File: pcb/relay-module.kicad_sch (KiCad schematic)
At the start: 12 parts

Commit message: initial checkin
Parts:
- added C1: .1uF, Capacitor_SMD:C_0603_1608Metric, symbol Device:C
- added D1: BAT48JFILM, Diode_SMD:D_SOD-323, symbol Diode:BAT48JFILM
- added J1: AVR-UPDI-6, Connector_PinHeader_2.54mm:PinHeader_2x03_P2.54mm_Vertical, symbol Connector:AVR-UPDI-6
- added J2: QWICC, Connector_JST:JST_SH_SM04B-SRSS-TB_1x04-1MP_P1.00mm_Horizontal, symbol CRGM Connector:QWIIC
- added J3: Power, Connector_JST:JST_SH_SM04B-SRSS-TB_1x04-1MP_P1.00mm_Horizontal, symbol CRGM Connector:JST-SH-4
- added JP1: Jumper_3_Open, Jumper:SolderJumper-3_P1.3mm_Open_RoundedPad1.0x1.5mm_NumberLabels, symbol Jumper:Jumper_3_Open
- added K1: PR24-5V-900-1A, CRG Makes:RELAY_PR24-5V-900-1A, symbol CRG Makes:PR24-5V-900-1A
- added MOV1: V250LA40BP, CRG Makes:V250LA40BP, symbol CRG Makes:MOV20D331K
- added P1, P2, P3, P4: MountingHole_Pad, MountingHole:MountingHole_3.2mm_M3_ISO14580_Pad, symbol Mechanical:MountingHole_Pad
- added Q1: MMBT3904, Package_TO_SOT_SMD:SOT-23, symbol Transistor_BJT:MMBT3904
- added R1, R2: 220, Resistor_SMD:R_0603_1608Metric, symbol Device:R_US
- added R3, R4: 10K, Resistor_SMD:R_0603_1608Metric, symbol Device:R_US
- added S1, S2: ~, CRGM Symbols:HIGH-VOLTAGE-5MM, symbol CRGM Symbols:High Voltage
- added U2: ATtiny1616-M, Package_DFN_QFN:VQFN-20-1EP_3x3mm_P0.4mm_EP1.7x1.7mm, symbol MCU_Microchip_ATtiny:ATtiny1616-M
- added U3: LTV-356T, Package_SO:SO-4_4.4x3.6mm_P2.54mm, symbol Isolator:LTV-356T
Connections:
- new net: R1.2, U3.1
- new net: R2.1, U3.3
- new net: JP1.1 (A), R3.2
- new net: JP1.3 (B), R4.2
- new net: Q1.1 (B), R2.2
- new net +3.3V: C1.1, J1.2 (VCC), J2.2, J3.4, JP1.2 (C), U2.4 (VCC), U3.4
- new net +5V: D1.1 (K), J3.1, K1.A1 (COIL1)
- new net GND: C1.2, J1.6 (GND), J2.1, J3.2, J3.3, Q1.2 (E), U2.21 (GND), U2.3 (GND), U3.2
- new net LOAD_IN: K1.COM_1 (COM1), P3.1
- new net LOAD_OUT: K1.NO, MOV1.P$1, P4.1
- new net NEUTRAL: MOV1.P$2, P1.1, P2.1
- new net RELAY_CONTROL: D1.2 (A), K1.A2 (COIL2), Q1.3 (C)
- new net RELAY_CTRL: R1.1, U2.15 (PC0)
- new net SCL: J2.4, R3.1, U2.14 (PB0)
- new net SDA: J2.3, R4.1, U2.13 (PB1)
- new net UPDI: J1.1 (DATA), U2.19 (~{RESET}/PA0)
- no-connect marks 0 -> 15
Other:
- removed sheet I2C Interface
- removed sheet Power
- removed sheet Relay
- note added: "Power Connector"
- note added: "Programming"
- note added: "QWICC / I2C"
- note added: "Relay"
- note added: "uC"
- moved on the sheet: FID1, FID2, FID3, H1, H2, H3, H4

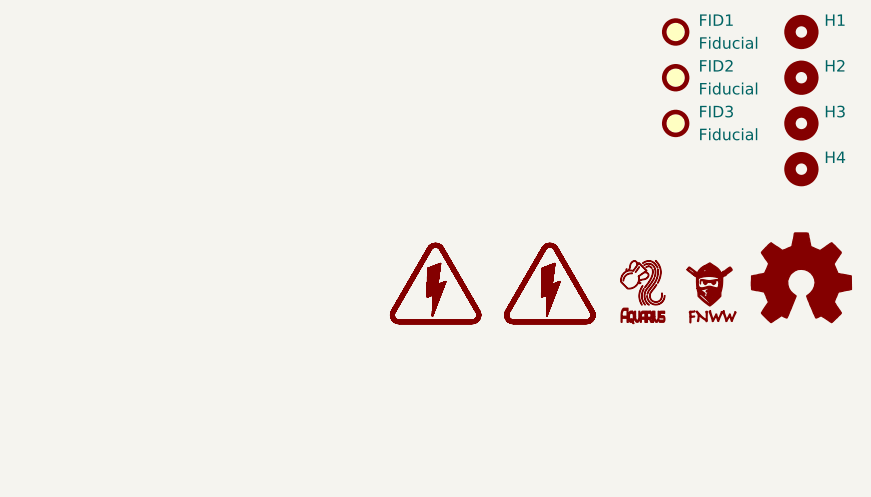
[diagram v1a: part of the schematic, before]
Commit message: Updated silkscreen
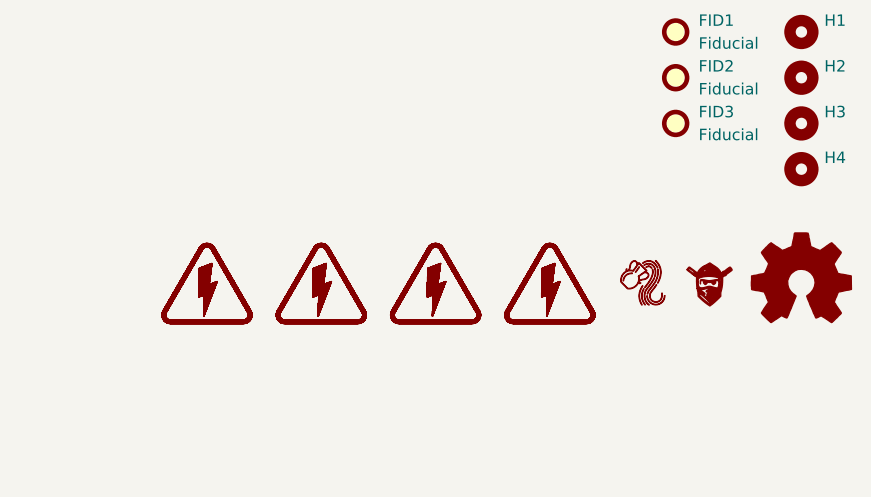
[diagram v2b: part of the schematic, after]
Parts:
- removed LOGO2: ~, CRGM Logos:Aquarius Name 2mmx5mm, symbol CRGM Logos:Aquarius Name
- removed LOGO4: ~, CRGM Logos:FNWW Name 2mmx5mm, symbol CRGM Logos:FNWW Name
- added S3, S4: ~, CRGM Symbols:HIGH-VOLTAGE-5MM, symbol CRGM Symbols:High Voltage
- LOGO1: footprint CRGM Logos:Aquarius Logo 5mm -> CRGM Logos:Aquarius Logo 10mm
- LOGO3: footprint CRGM Logos:FNWW Face 5mm -> CRGM Logos:FNWW Face 10mm
- LOGO5: footprint Symbol:OSHW-Symbol_6.7x6mm_SilkScreen -> Symbol:OSHW-Logo_5.7x6mm_SilkScreen
- S1, S2: now left out of the parts list
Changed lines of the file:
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@@
+	)
+	(symbol
+		(lib_id "CRGM Symbols:High Voltage")
+		(at 212.09 173.99 0)
+		(unit 1)
+		(exclude_from_sim no)
+		(in_bom no)
+		(on_board yes)
+		(dnp no)
+		(fields_autoplaced yes)
+		(property "Reference" "S3"
+			(at 212.09 183.388 0)
+			(effects
+				(font
+					(size 1.27 1.27)
+				)
+				(hide yes)
+			)
+		)
+		(property "Value" "~"
+			(at 212.09 173.99 0)
+			(effects
+				(font
+					(size 1.27 1.27)
+				)
+				(hide yes)
+			)
+		)
+		(property "Footprint" "CRGM Symbols:HIGH-VOLTAGE-5MM"
+			(at 213.36 181.102 0)
+			(effects
+				(font
+					(size 1.27 1.27)
+				)
+				(hide yes)
+			)
+		)
+		(property "Datasheet" ""
+			(at 212.09 173.99 0)
+			(effects
+				(font
+					(size 1.27 1.27)
+				)
+				(hide yes)
+			)
+		)
+		(property "Description" ""
+			(at 212.09 173.99 0)
+			(effects
+				(font
+					(size 1.27 1.27)
+				)
+				(hide yes)
+			)
+		)
+		(instances
+			(project "relay-module"
+				(path "/445c1fff-2e1a-48b1-a91f-a137832edebf"
+					(reference "S3")
+					(unit 1)
+				)
+			)
+		)
 	)
 	(symbol
@@
 			)
 		)
-		(property "Footprint" "CRGM Logos:Aquarius Logo 5mm"
+		(property "Footprint" "CRGM Logos:Aquarius Logo 10mm"
 			(at 261.874 179.578 0)
 			(effects
@@
 		(unit 1)
 		(exclude_from_sim no)
-		(in_bom yes)
+		(in_bom no)
 		(on_board yes)
 		(dnp no)
@@
 			)
 		)
-		(property "Footprint" "Symbol:OSHW-Symbol_6.7x6mm_SilkScreen"
+		(property "Footprint" "Symbol:OSHW-Logo_5.7x6mm_SilkScreen"
 			(at 278.13 173.99 0)
 			(effects
@@
 				(path "/445c1fff-2e1a-48b1-a91f-a137832edebf"
 					(reference "#PWR04")
-					(unit 1)
-				)
-			)
-		)
-	)
-	(symbol
-		(lib_id "CRGM Logos:Aquarius Name")
-		(at 260.3903 178.523 0)
-		(unit 1)
-		(exclude_from_sim no)
-		(in_bom no)
-		(on_board yes)
-		(dnp no)
-		(fields_autoplaced yes)
-		(property "Reference" "LOGO2"
-			(at 260.1363 179.539 0)
-			(effects
-				(font
-					(size 1.27 1.27)
-				)
-				(hide yes)
-			)
-		)
-		(property "Value" "~"
-			(at 258.1043 176.745 0)
-			(effects
-				(font
-					(size 1.27 1.27)
-				)
-				(hide yes)
-			)
-		)
-		(property "Footprint" "CRGM Logos:Aquarius Name 2mmx5mm"
-			(at 261.4063 181.063 0)
-			(effects
-				(font
-					(size 1.27 1.27)
-				)
-				(hide yes)
-			)
-		)
-		(property "Datasheet" ""
-			(at 258.1043 176.745 0)
-			(effects
-				(font
-					(size 1.27 1.27)
-				)
-				(hide yes)
-			)
-		)
-		(property "Description" ""
-			(at 258.1043 176.745 0)
-			(effects
-				(font
-					(size 1.27 1.27)
-				)
-				(hide yes)
-			)
-		)
-		(property "MPN" ""
-			(at 260.3903 178.523 0)
-			(effects
-				(font
-					(size 1.27 1.27)
-				)
-			)
-		)
-		(instances
-			(project ""
-				(path "/445c1fff-2e1a-48b1-a91f-a137832edebf"
-					(reference "LOGO2")
 					(unit 1)
 				)
@@
 	)
 	(symbol
-		(lib_id "CRGM Logos:FNWW Name")
-		(at 267.97 177.8 0)
-		(unit 1)
-		(exclude_from_sim no)
-		(in_bom no)
-		(on_board yes)
-		(dnp no)
-		(fields_autoplaced yes)
-		(property "Reference" "LOGO4"
-			(at 268.224 179.578 0)
-			(effects
-				(font
-					(size 1.27 1.27)
-				)
-				(hide yes)
-			)
-		)
-		(property "Value" "~"
-			(at 267.991 183.4101 0)
-			(effects
-				(font
-					(size 1.27 1.27)
-				)
-				(hide yes)
-			)
-		)
-		(property "Footprint" "CRGM Logos:FNWW Name 2mmx5mm"
-			(at 271.526 182.118 0)
-			(effects
-				(font
-					(size 1.27 1.27)
-				)
-				(hide yes)
-			)
-		)
-		(property "Datasheet" ""
-			(at 267.991 183.4101 0)
-			(effects
-				(font
-					(size 1.27 1.27)
-				)
-				(hide yes)
-			)
-		)
-		(property "Description" ""
-			(at 267.991 183.4101 0)
-			(effects
-				(font
-					(size 1.27 1.27)
-				)
-				(hide yes)
-			)
-		)
-		(property "MPN" ""
-			(at 267.97 177.8 0)
-			(effects
-				(font
-					(size 1.27 1.27)
-				)
-			)
-		)
-		(instances
-			(project ""
-				(path "/445c1fff-2e1a-48b1-a91f-a137832edebf"
-					(reference "LOGO4")
-					(unit 1)
-				)
-			)
-		)
-	)
-	(symbol
 		(lib_id "power:+3.3V")
 		(at 255.27 41.91 0)
@@
 			)
 		)
-		(property "Footprint" "CRGM Logos:FNWW Face 5mm"
+		(property "Footprint" "CRGM Logos:FNWW Face 10mm"
 			(at 267.97 179.578 0)
 			(effects
@@
 	)
 	(symbol
+		(lib_id "CRGM Symbols:High Voltage")
+		(at 224.79 173.99 0)
+		(unit 1)
+		(exclude_from_sim no)
+		(in_bom no)
+		(on_board yes)
+		(dnp no)
+		(fields_autoplaced yes)
+		(property "Reference" "S4"
+			(at 224.79 183.388 0)
+			(effects
+				(font
+					(size 1.27 1.27)
+				)
+				(hide yes)
+			)
+		)
+		(property "Value" "~"
+			(at 224.79 173.99 0)
+			(effects
+				(font
+					(size 1.27 1.27)
+				)
+				(hide yes)
+			)
+		)
+		(property "Footprint" "CRGM Symbols:HIGH-VOLTAGE-5MM"
+			(at 226.06 181.102 0)
+			(effects
+				(font
+					(size 1.27 1.27)
+				)
+				(hide yes)
+			)
+		)
+		(property "Datasheet" ""
+			(at 224.79 173.99 0)
+			(effects
+				(font
+					(size 1.27 1.27)
+				)
+				(hide yes)
+			)
+		)
+		(property "Description" ""
+			(at 224.79 173.99 0)
+			(effects
+				(font
+					(size 1.27 1.27)
+				)
+				(hide yes)
+			)
+		)
+		(instances
+			(project "relay-module"
+				(path "/445c1fff-2e1a-48b1-a91f-a137832edebf"
+					(reference "S4")
+					(unit 1)
+				)
+			)
+		)
+	)
+	(symbol
 		(lib_id "Device:R_US")
 		(at 262.89 52.07 180)
@@
 		(unit 1)
 		(exclude_from_sim no)
-		(in_bom yes)
-		(on_board yes)
-		(dnp no)
+		(in_bom no)
+		(on_board yes)
+		(dnp no)

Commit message: v1.0 Relay Module Panel 2x2
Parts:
- removed FID1, FID2, FID3: Fiducial, Fiducial:Fiducial_0.75mm_Mask1.5mm, symbol Mechanical:Fiducial
- added C2: .1uF, Capacitor_SMD:C_0603_1608Metric, symbol Device:C
- added J4: Power Out, CRGM Connector:SM04B-SRSS-TB, symbol CRGM Connector:JST-SH-4
- C1: LCSC_PN C66501 -> (none); MN_PN CL10B104KO8NNNC -> (none)
- D1: LCSC_PN C155590 -> (none)
- H1, H2, H3, H4, JP1, LOGO5, P1, P2, P3, P4, S1, S2, S3, S4: now not fitted
- J1: now not fitted; now left out of the parts list
- J2: footprint Connector_JST:JST_SH_SM04B-SRSS-TB_1x04-1MP_P1.00mm_Horizontal -> CRGM Connector:SM04B-SRSS-TB; LCSC (none) -> C2763614; LCSC_PN C2763614 -> (none); MN (none) -> JST; MPN (none) -> SM04B-SRSS-TB
- J3: value Power -> Power In; footprint Connector_JST:JST_SH_SM04B-SRSS-TB_1x04-1MP_P1.00mm_Horizontal -> CRGM Connector:SM04B-SRSS-TB
- K1: LCSC (none) -> C7029760; LCSC_PN C7029760 -> (none); MN (none) -> Same Sky; MPN (none) -> PR24-5V-900-1A
- LOGO1: footprint CRGM Logos:Aquarius Logo 10mm -> CRGM Logos:Aquarius Logo 5mm; now not fitted
- LOGO3: footprint CRGM Logos:FNWW Face 10mm -> CRGM Logos:FNWW Face 5mm; now not fitted
- MOV1: LCSC (none) -> C1527448; LCSC_PN C1527448 -> (none); MN (none) -> Littlefuse; MPN (none) -> V250LA40BP; now in the parts list
- Q1: LCSC (none) -> C909754; LCSC_PN C909754 -> (none); MPN (none) -> MMBT3904
- R1, R2: LCSC_PN C1226 -> (none)
- R3, R4: LCSC_PN C2930027 -> (none)
- U2: footprint Package_DFN_QFN:VQFN-20-1EP_3x3mm_P0.4mm_EP1.7x1.7mm -> CRG Makes:VQFN-20-1EP_3x3mm_P0.4mm_EP1.7x1.7mm_ThermalVias; LCSC_PN C507118 -> (none)
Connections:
- net +3.3V: now also J4.4
- net +5V: now also C2.1, J4.1
- net GND: now also C2.2, J4.2, J4.3

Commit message: Updated for panelization.
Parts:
- added TP1: RELAY_CONTROL, TestPoint:TestPoint_Pad_D1.0mm, symbol Connector:TestPoint
- added TP2: RELAY_CTRL, TestPoint:TestPoint_Pad_D1.0mm, symbol Connector:TestPoint
- added TP3: UPDI, TestPoint:TestPoint_Pad_D1.0mm, symbol Connector:TestPoint
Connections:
- net RELAY_CONTROL: now also TP1.1
- net RELAY_CTRL: now also TP2.1
- net UPDI: now also TP3.1

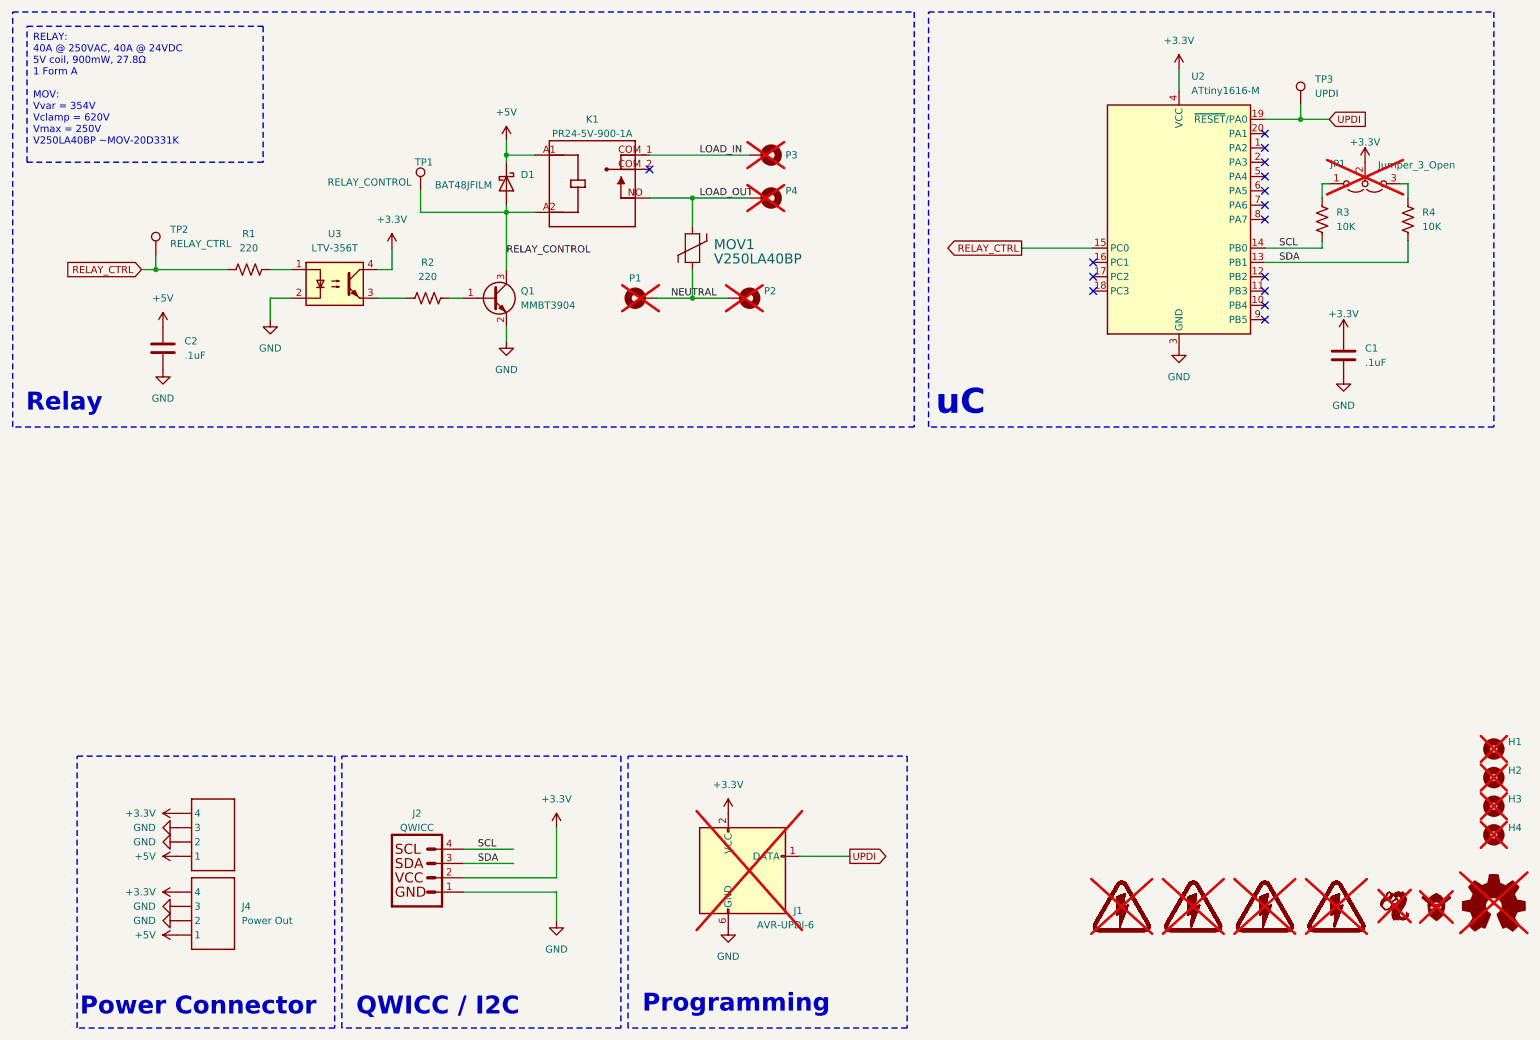
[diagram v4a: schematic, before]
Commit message: Added power, relay LEDs
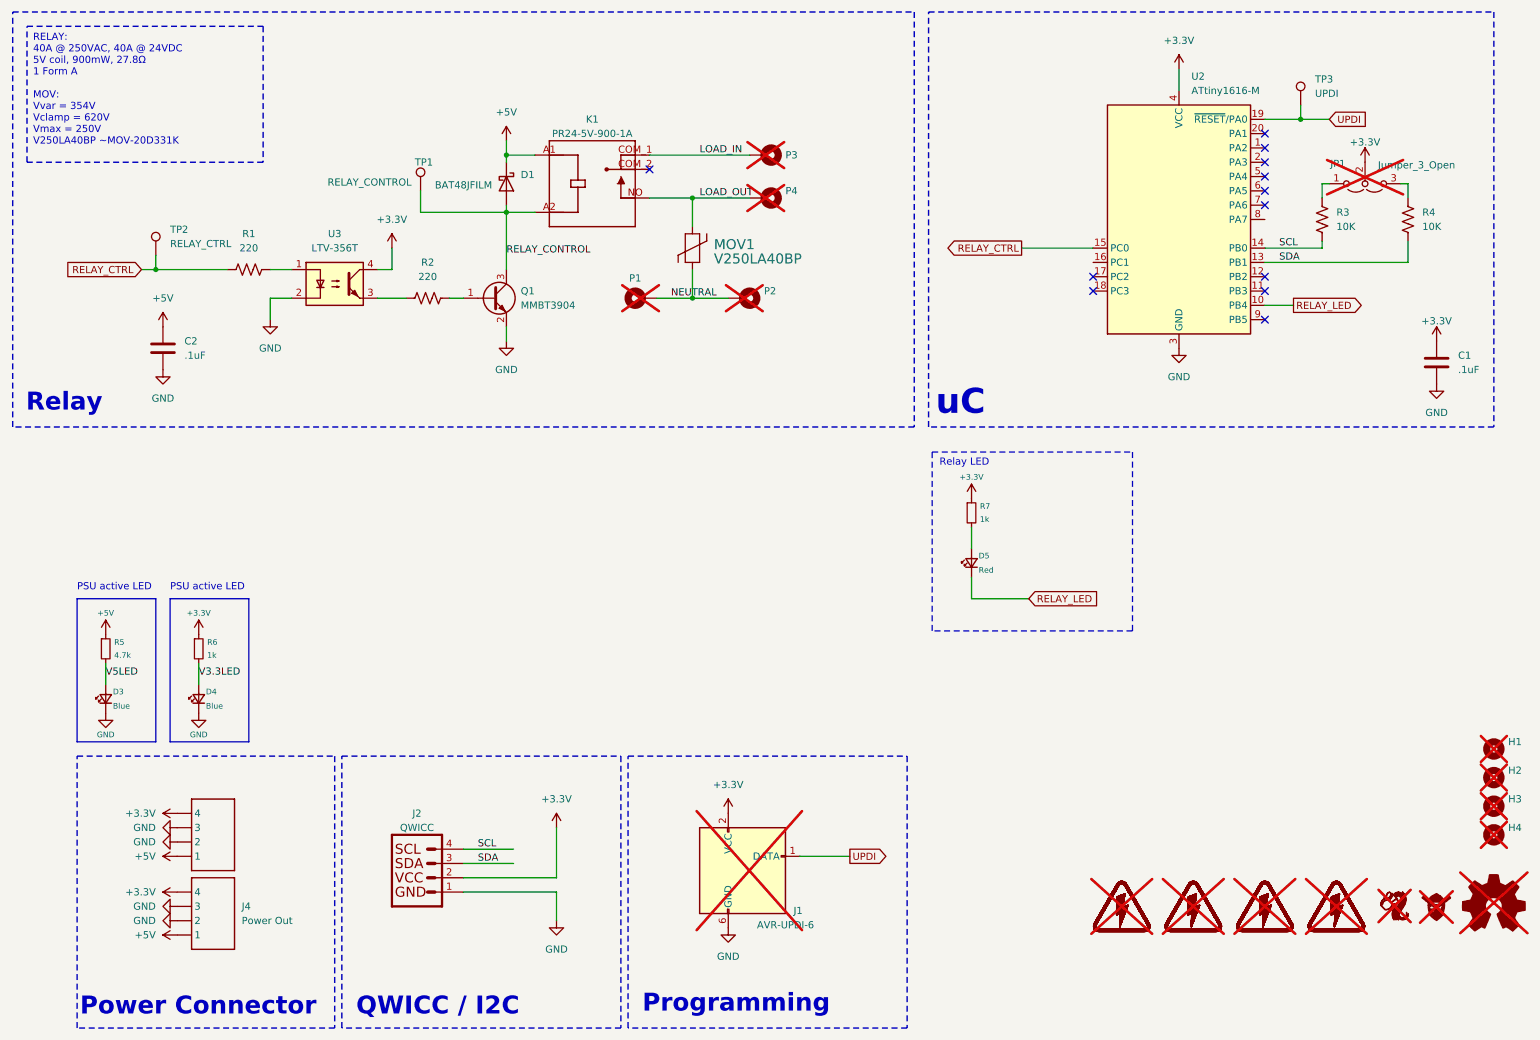
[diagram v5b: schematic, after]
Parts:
- added D3, D4: Blue, LED_SMD:LED_0603_1608Metric, symbol Device:LED_Small
- added D5: Red, LED_SMD:LED_0603_1608Metric, symbol Device:LED_Small
- added R5: 4.7k, Resistor_SMD:R_0603_1608Metric, symbol Device:R_Small
- added R6, R7: 1k, Resistor_SMD:R_0603_1608Metric, symbol Device:R_Small
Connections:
- net +3.3V: now also R6.1, R7.1
- net +5V: now also R5.1
- net GND: now also D3.1 (K), D4.1 (K)
- net RELAY_LED: now reaches U2.10 (PB4)
- net RELAY_LED: now also D5.1 (K)
- new net: D5.2 (A), R7.2
- new net V3.3LED: D4.2 (A), R6.2
- new net V5LED: D3.2 (A), R5.2
- no-connect marks 15 -> 12
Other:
- note added: "PSU active LED"
- note added: "Relay LED"
- moved on the sheet: C1

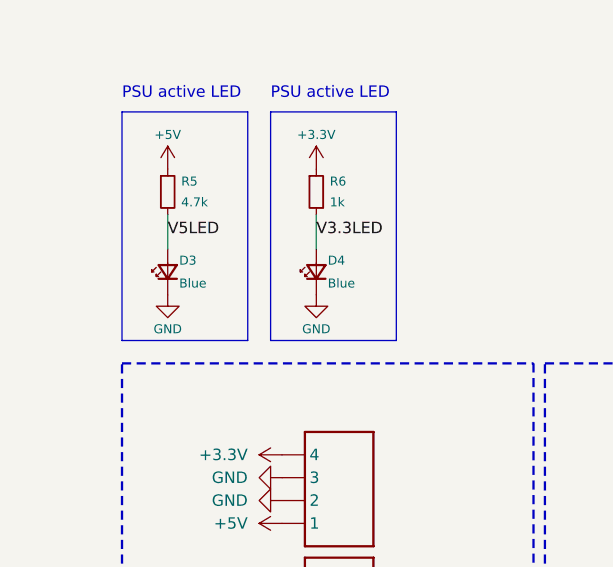
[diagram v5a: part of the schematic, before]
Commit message: Changed 5v to orange LED
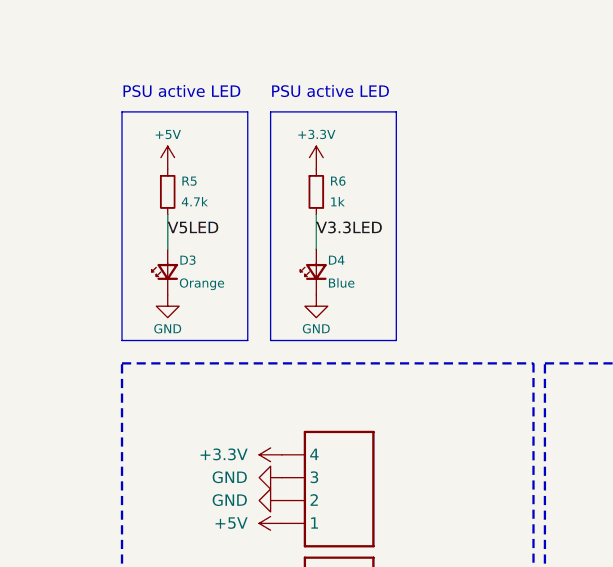
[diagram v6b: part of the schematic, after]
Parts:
- D3: value Blue -> Orange; Digikey 5962-XL-1608UBC-04TR-ND -> 5962-XL-1608UOC-06TR-ND; LCSC C965807 -> C965800; MPN XL-1608UBC-04 -> XL-1608UOC-06; Mouser 710-150060BS75020 -> 859-LTST-C190KFKT
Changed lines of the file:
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@@
 			)
 		)
-		(property "Value" "Blue"
+		(property "Value" "Orange"
 			(at 33.02 138.43 90)
 			(effects
@@
 			)
 		)
-		(property "Description" "20mA 240mcd Colorless Blue 120° 70mW 3.3V 0603"
+		(property "Description" "20mA 315mcd Colorless Orange 120° 50mW 2.3V 0603"
 			(at 31.75 137.16 0)
 			(effects
@@
 			)
 		)
-		(property "MPN" "XL-1608UBC-04"
+		(property "MPN" "XL-1608UOC-06"
 			(at 31.75 137.16 0)
 			(effects
@@
 			)
 		)
-		(property "Mouser" "710-150060BS75020"
+		(property "Mouser" "859-LTST-C190KFKT"
 			(at 31.75 137.16 0)
 			(effects
@@
 			)
 		)
-		(property "Digikey" "5962-XL-1608UBC-04TR-ND"
+		(property "Digikey" "5962-XL-1608UOC-06TR-ND"
 			(at 31.75 137.16 0)
 			(effects
@@
 			)
 		)
-		(property "LCSC" "C965807"
+		(property "LCSC" "C965800"
 			(at 31.75 137.16 0)
 			(effects
